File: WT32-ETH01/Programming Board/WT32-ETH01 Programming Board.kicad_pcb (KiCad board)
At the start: 2 copper layers, 48.3 x 83.8 mm, 0 parts

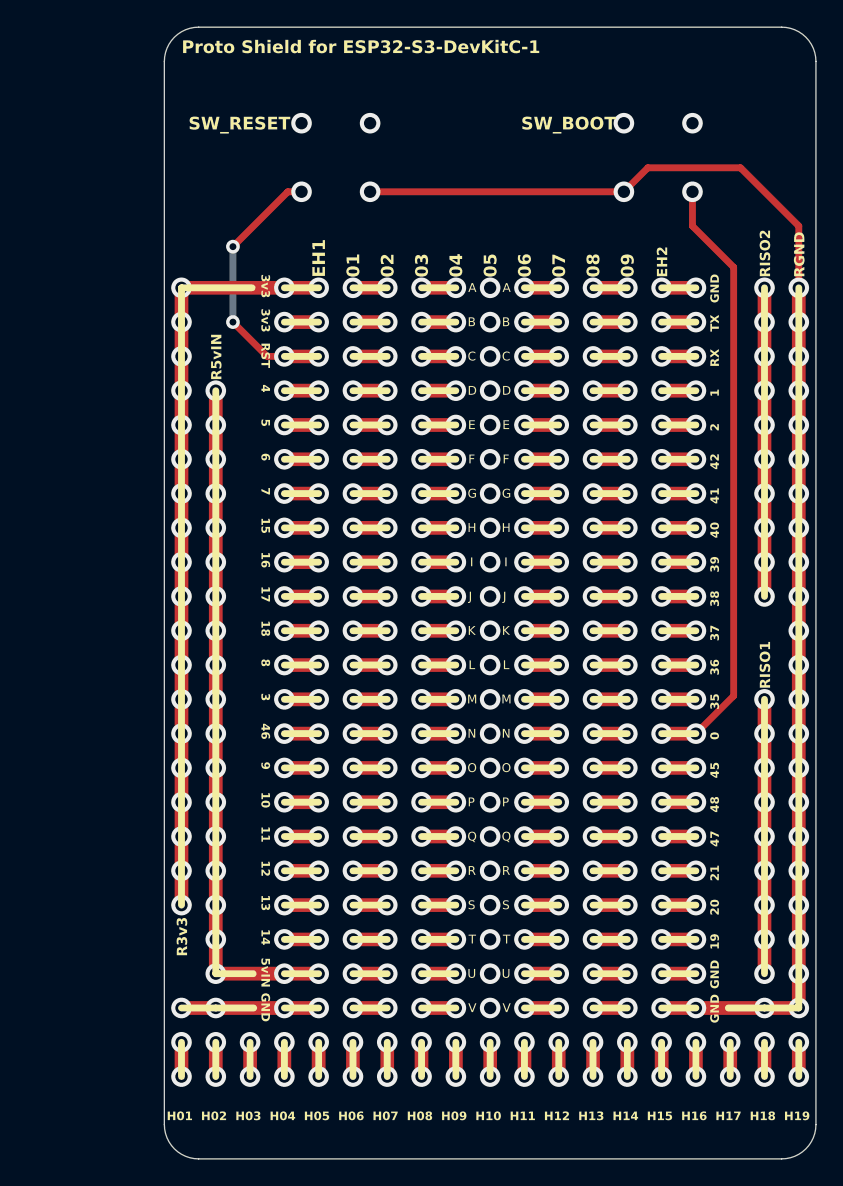
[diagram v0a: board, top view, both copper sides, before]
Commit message: V00.02.00 of WT32-ETH01 programming/proto board ordered
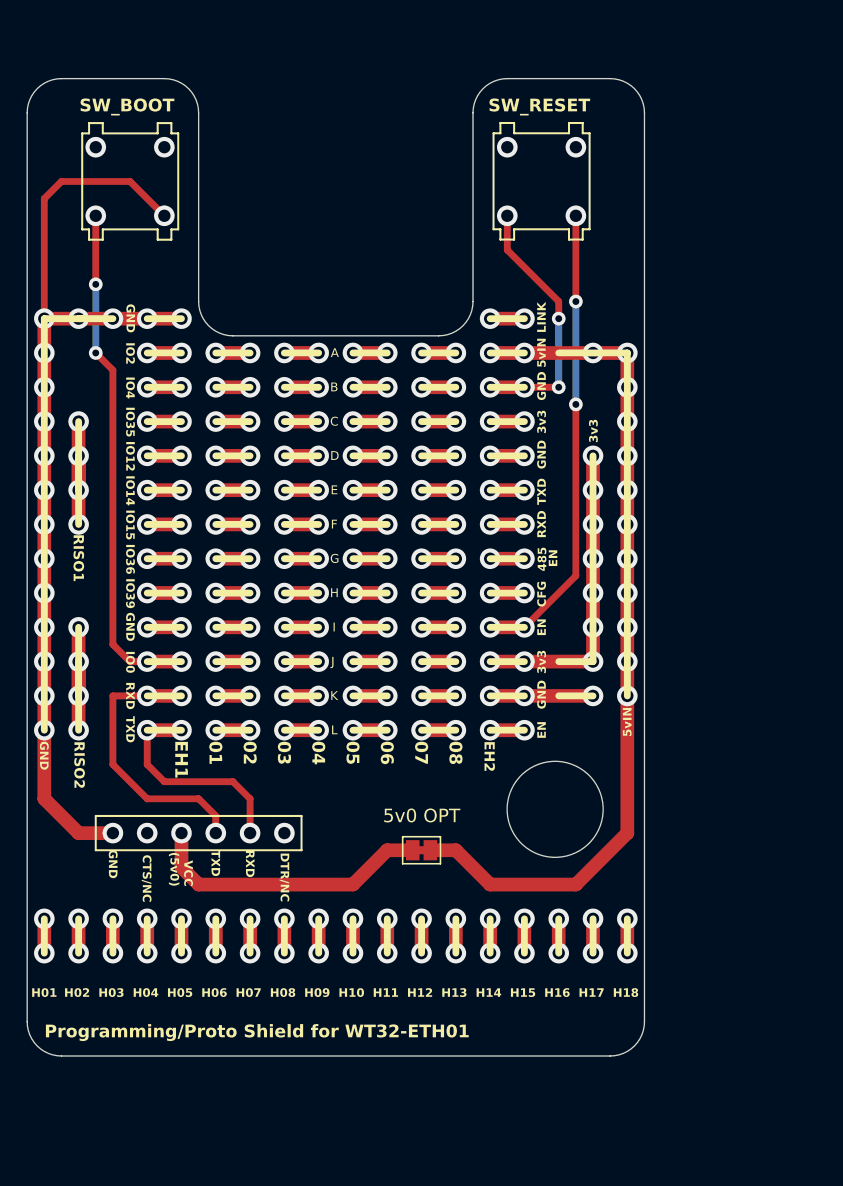
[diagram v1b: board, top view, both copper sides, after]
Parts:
- added 5v0 OPT: SolderJumper-2_P1.3mm_Bridged_Pad1.0x1.5mm, Jumper:SolderJumper-2_P1.3mm_Bridged_Pad1.0x1.5mm, F.Cu at (44.5, 76.2)
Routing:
- net (no net): track 695.5 -> 546.3 mm, vias 415 -> 247
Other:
- board size 48.3 x 83.8 mm -> 45.7 x 72.4 mm
- board text added: "485"
- board text added: "CFG"
- board text added: "CTS/NC"
- board text added: "DTR/NC"
- board text added: "EN"
- board text added: "IO0"
- board text added: "IO12"
- board text added: "IO14"
- board text added: "IO15"
- board text added: "IO2"
- board text added: "IO35"
- board text added: "IO36"
- board text added: "IO39"
- board text added: "IO4"
- board text added: "LINK"
- board text added: "M/N: JDS2.COM/AAB/002"
- board text added: "Programming/Proto Shield for WT32-ETH01"
- board text added: "RXD"
- board text added: "TXD"
- board text added: "VCC (5v0)"
- board text added: "VER: 00.02.00"
- board text removed: "0"
- board text removed: "09"
- board text removed: "1"
- board text removed: "10"
- board text removed: "11"
- board text removed: "12"
- board text removed: "13"
- board text removed: "14"
- board text removed: "15"
- board text removed: "16"
- board text removed: "17"
- board text removed: "18"
- board text removed: "19"
- board text removed: "2"
- board text removed: "20"
- board text removed: "21"
- board text removed: "3"
- board text removed: "35"
- board text removed: "36"
- board text removed: "37"
- board text removed: "38"
- board text removed: "39"
- board text removed: "4"
- board text removed: "40"
- board text removed: "41"
- board text removed: "42"
- board text removed: "45"
- board text removed: "46"
- board text removed: "47"
- board text removed: "48"
- board text removed: "5"
- board text removed: "6"
- board text removed: "7"
- board text removed: "8"
- board text removed: "9"
- board text removed: "H19"
- board text removed: "M"
- board text removed: "M/N: JDS2.COM/AAB/001"
- board text removed: "N"
- board text removed: "O"
- board text removed: "P"
- board text removed: "Proto Shield for ESP32-S3-DevKitC-1"
- board text removed: "Q"
- board text removed: "R"
- board text removed: "R3v3"
- board text removed: "R5vIN"
- board text removed: "RGND"
- board text removed: "RST"
- board text removed: "RX"
- board text removed: "S"
- board text removed: "T"
- board text removed: "TX"
- board text removed: "U"
- board text removed: "V"
- board text removed: "VER: 01.00.00"

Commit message: Fix buttons, ver number, spacing, labels
- Space header labels slightly further from center so can be seen when headers installed
- Update version number
- A tiny tiny bit more spacing to the ETH jack on mounted board
- Fix button through-hole size to slightly larger
- Fix button spacing to wider + taller for normal bent legs
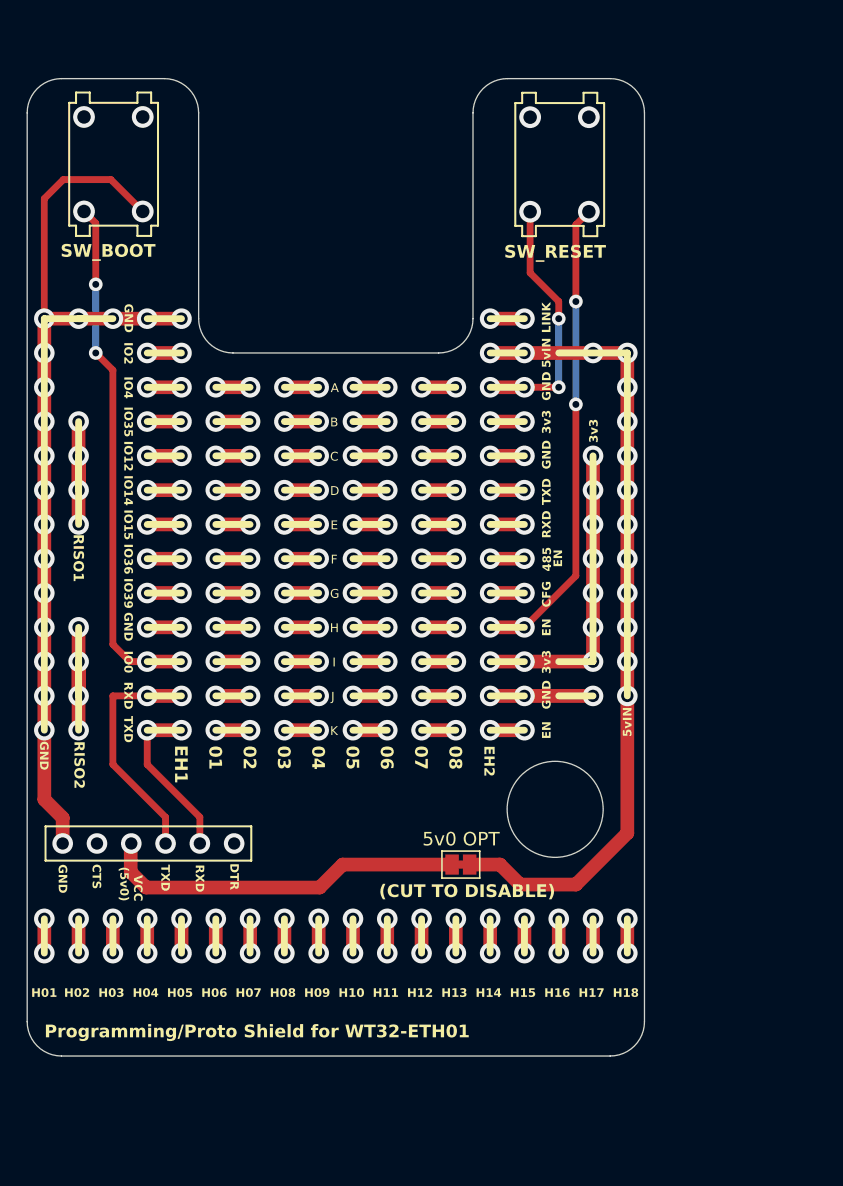
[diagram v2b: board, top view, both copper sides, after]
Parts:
- moved 5v0 OPT 3.10 mm to (47.4, 77.3)
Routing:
- net (no net): track 546.3 -> 528.5 mm, vias 247 -> 239
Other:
- outline, holes or cut-outs redrawn
- board text added: "(CUT TO DISABLE)"
- board text added: "CTS"
- board text added: "DTR"
- board text added: "VER: 01.00.00"
- board text removed: "CTS/NC"
- board text removed: "DTR/NC"
- board text removed: "L"
- board text removed: "VER: 00.02.00"
